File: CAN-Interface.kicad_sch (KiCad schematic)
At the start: 9 parts, among them J2 Conn_01x04_Socket, U6 SN65HVD231

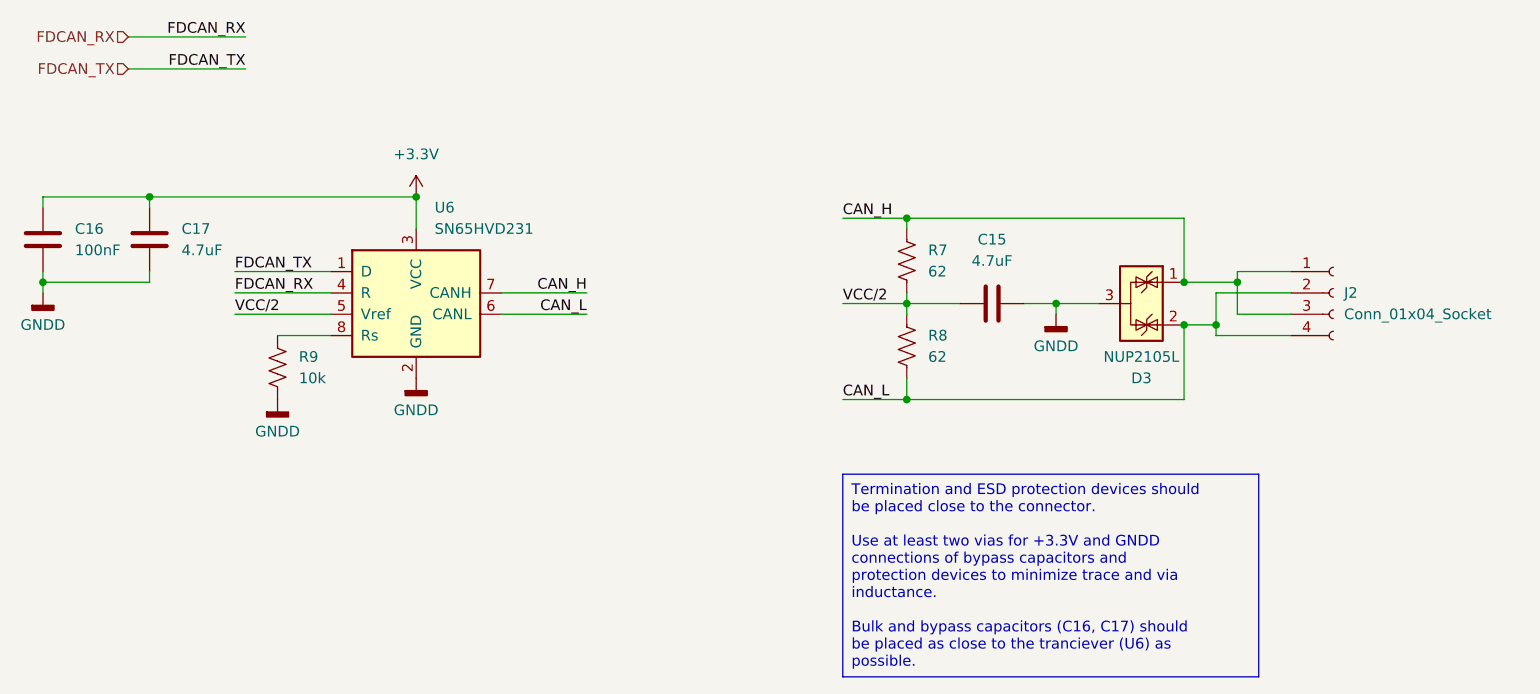
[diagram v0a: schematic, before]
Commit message: New, simpler CAN interface that supports FD CAN
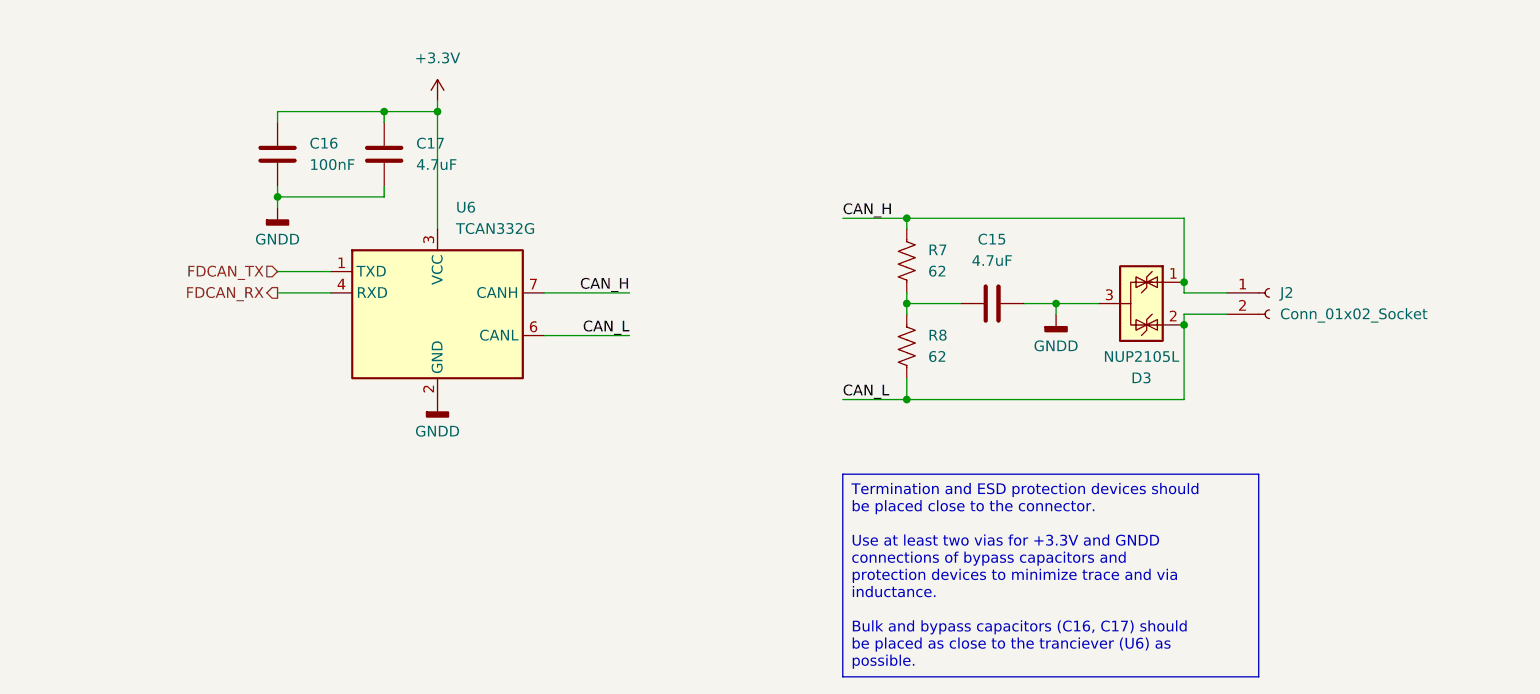
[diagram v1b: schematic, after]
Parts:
- removed J2: Conn_01x04_Socket, symbol Connector:Conn_01x04_Socket
- removed R9: 10k, Resistor_SMD:R_0603_1608Metric_Pad0.98x0.95mm_HandSolder, symbol Device:R_US
- removed U6: SN65HVD231, Package_SO:SOIC-8_3.9x4.9mm_P1.27mm, symbol Interface_CAN_LIN:SN65HVD231
- added J2: Conn_01x02_Socket, symbol Connector:Conn_01x02_Socket
- added U6: TCAN332G, symbol Interface_CAN_LIN:TCAN332G
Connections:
- net +3.3V: now also U6.3 (VCC)
- net CAN_H: now also J2.1 (Pin_1), U6.7 (CANH)
- net CAN_L: now also J2.2 (Pin_2), U6.6 (CANL)
- net FDCAN_RX: now also U6.4 (RXD)
- net FDCAN_TX: now also U6.1 (TXD)
- net GNDD: now also U6.2 (GND)
- net VCC/2: no longer names the net of C15.1, R7.2, R8.1
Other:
- moved on the sheet: C16, C17

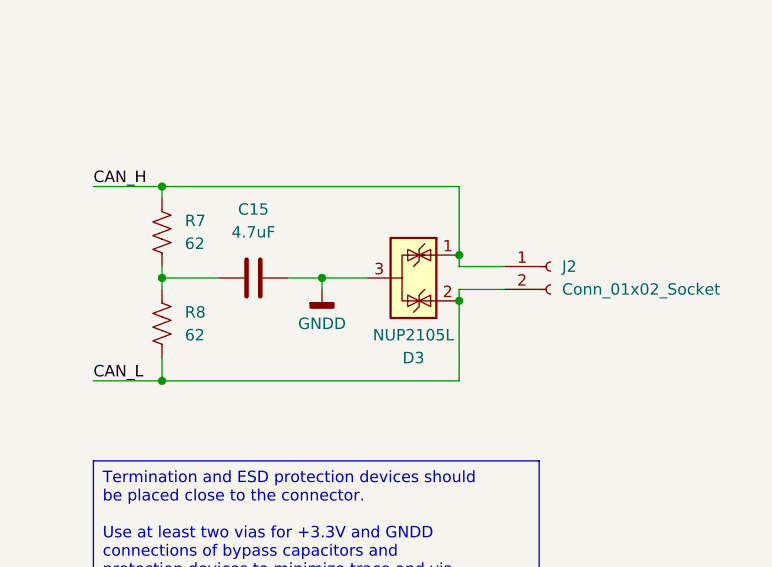
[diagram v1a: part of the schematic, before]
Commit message: Routed USB interface from port to MCU and CAN interface from connector to transceiver
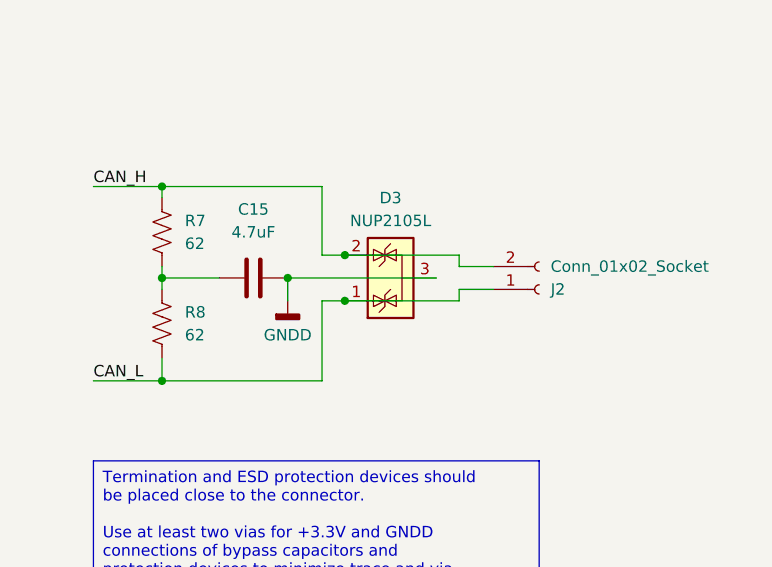
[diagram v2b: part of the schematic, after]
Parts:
- J2: footprint (none) -> TerminalBlock_Phoenix:TerminalBlock_Phoenix_MKDS-1,5-2-5.08_1x02_P5.08mm_Horizontal
- U6: footprint (none) -> Package_SO:SOIC-8_3.9x4.9mm_P1.27mm
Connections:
- net CAN_H: now also D3.2 (K), J2.2 (Pin_2); no longer D3.1 (K), J2.1 (Pin_1)
- net CAN_L: now also D3.1 (K), J2.1 (Pin_1); no longer D3.2 (K), J2.2 (Pin_2)
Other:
- moved on the sheet: D3
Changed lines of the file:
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@@
 	(paper "A4")
 	(junction
-		(at 176.53 93.98)
+		(at 179.07 91.44)
 		(diameter 0)
 		(color 0 0 0 0)
@@
 	)
 	(junction
+		(at 179.07 96.52)
+		(diameter 0)
+		(color 0 0 0 0)
+	)
+	(junction
 		(at 83.82 81.28)
 		(diameter 0)
@@
 	)
 	(junction
-		(at 191.77 96.52)
-		(diameter 0)
-		(color 0 0 0 0)
-	)
-	(junction
 		(at 158.75 93.98)
 		(diameter 0)
@@
 	)
 	(junction
-		(at 191.77 91.44)
-		(diameter 0)
-		(color 0 0 0 0)
-	)
-	(junction
 		(at 102.87 71.12)
 		(diameter 0)
 		(color 0 0 0 0)
 	)
-	(wire
-		(pts
-			(xy 158.75 83.82) (xy 191.77 83.82)
+	(junction
+		(at 172.72 93.98)
+		(diameter 0)
+		(color 0 0 0 0)
+	)
+	(wire
+		(pts
+			(xy 176.53 96.52) (xy 176.53 105.41)
+		)
+		(stroke
+			(width 0)
+			(type default)
+		)
+	)
+	(wire
+		(pts
+			(xy 158.75 83.82) (xy 176.53 83.82)
 		)
 		(stroke
@@
 	(wire
 		(pts
-			(xy 191.77 96.52) (xy 191.77 105.41)
-		)
-		(stroke
-			(width 0)
-			(type default)
-		)
-	)
-	(wire
-		(pts
-			(xy 172.72 93.98) (xy 176.53 93.98)
-		)
-		(stroke
-			(width 0)
-			(type default)
-		)
-	)
-	(wire
-		(pts
-			(xy 191.77 92.71) (xy 196.85 92.71)
-		)
-		(stroke
-			(width 0)
-			(type default)
-		)
-	)
-	(wire
-		(pts
-			(xy 191.77 95.25) (xy 191.77 96.52)
+			(xy 179.07 96.52) (xy 176.53 96.52)
+		)
+		(stroke
+			(width 0)
+			(type default)
+		)
+	)
+	(wire
+		(pts
+			(xy 179.07 96.52) (xy 191.77 96.52)
 		)
 		(stroke
@@
 	(wire
 		(pts
-			(xy 176.53 93.98) (xy 176.53 95.25)
+			(xy 172.72 93.98) (xy 172.72 96.52)
 		)
 		(stroke
@@
 	(wire
 		(pts
+			(xy 172.72 93.98) (xy 189.23 93.98)
+		)
+		(stroke
+			(width 0)
+			(type default)
+		)
+	)
+	(wire
+		(pts
+			(xy 191.77 92.71) (xy 191.77 91.44)
+		)
+		(stroke
+			(width 0)
+			(type default)
+		)
+	)
+	(wire
+		(pts
 			(xy 158.75 105.41) (xy 158.75 102.87)
 		)
@@
 	(wire
 		(pts
-			(xy 191.77 83.82) (xy 191.77 91.44)
+			(xy 195.58 92.71) (xy 191.77 92.71)
 		)
 		(stroke
@@
 	(wire
 		(pts
-			(xy 181.61 93.98) (xy 176.53 93.98)
+			(xy 179.07 91.44) (xy 176.53 91.44)
 		)
 		(stroke
@@
 	(wire
 		(pts
-			(xy 158.75 105.41) (xy 191.77 105.41)
-		)
-		(stroke
-			(width 0)
-			(type default)
-		)
-	)
-	(wire
-		(pts
-			(xy 191.77 95.25) (xy 196.85 95.25)
+			(xy 158.75 105.41) (xy 176.53 105.41)
+		)
+		(stroke
+			(width 0)
+			(type default)
+		)
+	)
+	(wire
+		(pts
+			(xy 191.77 95.25) (xy 195.58 95.25)
+		)
+		(stroke
+			(width 0)
+			(type default)
+		)
+	)
+	(wire
+		(pts
+			(xy 179.07 91.44) (xy 191.77 91.44)
 		)
 		(stroke
@@
 	(wire
 		(pts
+			(xy 176.53 91.44) (xy 176.53 83.82)
+		)
+		(stroke
+			(width 0)
+			(type default)
+		)
+	)
+	(wire
+		(pts
 			(xy 83.82 71.12) (xy 96.52 71.12)
 		)
@@
 	(wire
 		(pts
-			(xy 191.77 91.44) (xy 191.77 92.71)
+			(xy 191.77 96.52) (xy 191.77 95.25)
 		)
 		(stroke
@@
 	(symbol
 		(lib_id "Power_Protection:NUP2105L")
-		(at 186.69 93.98 270)
+		(at 184.15 93.98 90)
 		(unit 1)
 		(exclude_from_sim no)
@@
 		(fields_autoplaced yes)
 		(property "Reference" "D3"
-			(at 186.69 102.87 90)
+			(at 184.15 85.09 90)
 			(effects
 				(font
@@
 		)
 		(property "Value" "NUP2105L"
-			(at 186.69 100.33 90)
+			(at 184.15 87.63 90)
 			(effects
 				(font
@@
 		)
 		(property "Footprint" "Package_TO_SOT_SMD:SOT-23"
-			(at 185.42 99.695 0)
+			(at 185.42 88.265 0)
 			(effects
 				(font
@@
 		)
 		(property "Datasheet" "https://www.onsemi.com/pub_link/Collateral/NUP2105L-D.PDF"
-			(at 189.865 97.155 0)
+			(at 180.975 90.805 0)
 			(effects
 				(font
@@
 		)
 		(property "Description" "Dual Line CAN Bus Protector, 24Vrwm"
-			(at 186.69 93.98 0)
+			(at 184.15 93.98 0)
 			(effects
 				(font
@@
 	(symbol
 		(lib_id "power:GNDD")
-		(at 176.53 95.25 0)
+		(at 172.72 96.52 0)
 		(unit 1)
 		(exclude_from_sim no)
@@
 		(fields_autoplaced yes)
 		(property "Reference" "#PWR034"
-			(at 176.53 101.6 0)
+			(at 172.72 102.87 0)
 			(effects
 				(font
@@
 		)
 		(property "Value" "GNDD"
-			(at 176.53 99.06 0)
+			(at 172.72 100.33 0)
 			(effects
 				(font
@@
 		)
 		(property "Footprint" ""
-			(at 176.53 95.25 0)
+			(at 172.72 96.52 0)
 			(effects
 				(font
@@
 		)
 		(property "Datasheet" ""
-			(at 176.53 95.25 0)
+			(at 172.72 96.52 0)
 			(effects
 				(font
@@
 		)
 		(property "Description" "Power symbol creates a global label with name \"GNDD\" , digital ground"
-			(at 176.53 95.25 0)
+			(at 172.72 96.52 0)
 			(effects
 				(font
@@
 	)
 	(symbol
-		(lib_id "Connector:Conn_01x02_Socket")
-		(at 201.93 92.71 0)
-		(unit 1)
-		(exclude_from_sim no)
-		(in_bom yes)
-		(on_board yes)
-		(dnp no)
-		(fields_autoplaced yes)
-		(property "Reference" "J2"
-			(at 203.2 92.7099 0)
-			(effects
-				(font
-					(size 1.27 1.27)
-				)
-				(justify left)
-			)
-		)
-		(property "Value" "Conn_01x02_Socket"
-			(at 203.2 95.2499 0)
-			(effects
-				(font
-					(size 1.27 1.27)
-				)
-				(justify left)
-			)
-		)
-		(property "Footprint" ""
-			(at 201.93 92.71 0)
-			(effects
-				(font
-					(size 1.27 1.27)
-				)
-				(hide yes)
-			)
-		)
-		(property "Datasheet" "~"
-			(at 201.93 92.71 0)
-			(effects
-				(font
-					(size 1.27 1.27)
-				)
-				(hide yes)
-			)
-		)
-		(property "Description" "Generic connector, single row, 01x02, script generated"
-			(at 201.93 92.71 0)
-			(effects
-				(font
-					(size 1.27 1.27)
-				)
-				(hide yes)
-			)
-		)
-		(pin "2"
-		)
-		(pin "1"
-		)
-		(instances
-			(project ""
-				(path "/c41b490b-5ab6-4438-aea0-388670bb08f4/60cb3ed2-d119-4f53-8d04-570ad94c5f39"
-					(reference "J2")
-					(unit 1)
-				)
-			)
-		)
-	)
-	(symbol
 		(lib_id "Device:C")
 		(at 168.91 93.98 90)
@@
 				(path "/c41b490b-5ab6-4438-aea0-388670bb08f4/60cb3ed2-d119-4f53-8d04-570ad94c5f39"
 					(reference "C15")
+					(unit 1)
+				)
+			)
+		)
+	)
+	(symbol
+		(lib_id "Connector:Conn_01x02_Socket")
+		(at 200.66 95.25 0)
+		(mirror x)
+		(unit 1)
+		(exclude_from_sim no)
+		(in_bom yes)
+		(on_board yes)
+		(dnp no)
+		(property "Reference" "J2"
+			(at 201.93 95.2501 0)
+			(effects
+				(font
+					(size 1.27 1.27)
+				)
+				(justify left)
+			)
+		)
+		(property "Value" "Conn_01x02_Socket"
+			(at 201.93 92.7101 0)
+			(effects
+				(font
+					(size 1.27 1.27)
+				)
+				(justify left)
+			)
+		)
+		(property "Footprint" "TerminalBlock_Phoenix:TerminalBlock_Phoenix_MKDS-1,5-2-5.08_1x02_P5.08mm_Horizontal"
+			(at 200.66 95.25 0)
+			(effects
+				(font
+					(size 1.27 1.27)
+				)
+				(hide yes)
+			)
+		)
+		(property "Datasheet" "~"
+			(at 200.66 95.25 0)
+			(effects
+				(font
+					(size 1.27 1.27)
+				)
+				(hide yes)
+			)
+		)
+		(property "Description" "Generic connector, single row, 01x02, script generated"
+			(at 200.66 95.25 0)
+			(effects
+				(font
+					(size 1.27 1.27)
+				)
+				(hide yes)
+			)
+		)
+		(pin "2"
+		)
+		(pin "1"
+		)
+		(instances
+			(project "SRAD-Avionics"
+				(path "/c41b490b-5ab6-4438-aea0-388670bb08f4/60cb3ed2-d119-4f53-8d04-570ad94c5f39"
+					(reference "J2")
 					(unit 1)
 				)
@@
 			)
 		)
-		(property "Footprint" ""
+		(property "Footprint" "Package_SO:SOIC-8_3.9x4.9mm_P1.27mm"
 			(at 102.87 107.95 0)
 			(effects
